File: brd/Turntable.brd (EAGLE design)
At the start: 100 x 80 mm, 115 parts, among them CON1 Pannel, CON2 CAN, CON3 Turntable, CON4 STEPPER_CON, CON5 STEPPER_CON, CON8 SPK, IC1 7805, IC2 LM393N, J1 MiniStp2, J10 MiniStp1, Q1 BS170, SW1 EC12E_SW, U2 LED NANO, X1 AK500/2+M, X2 AK500/2+M, X3 MAB 5SH Conrad: 738247 - VQ, X4 AK500/2+M, X5 Reichelt MEBP 8-8S

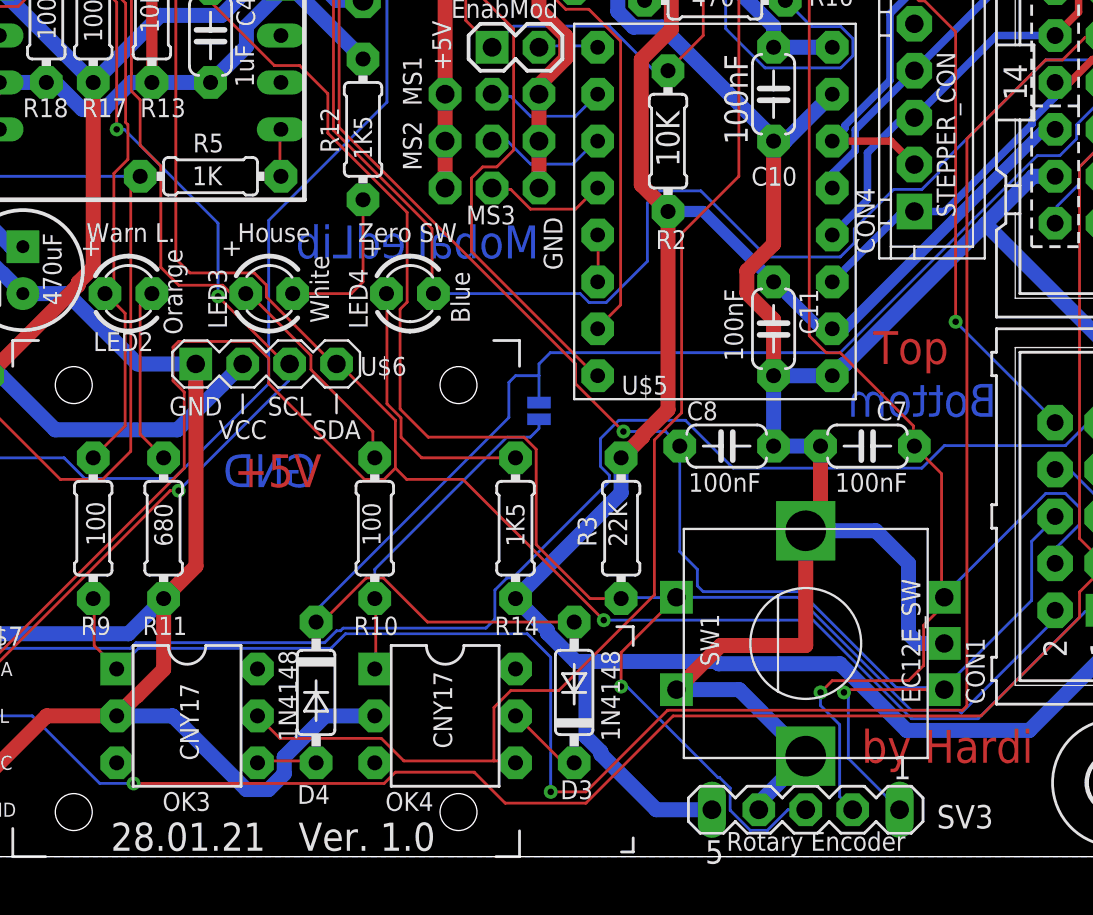
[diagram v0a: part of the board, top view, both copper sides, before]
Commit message: Corrected Potary Encoder Pins
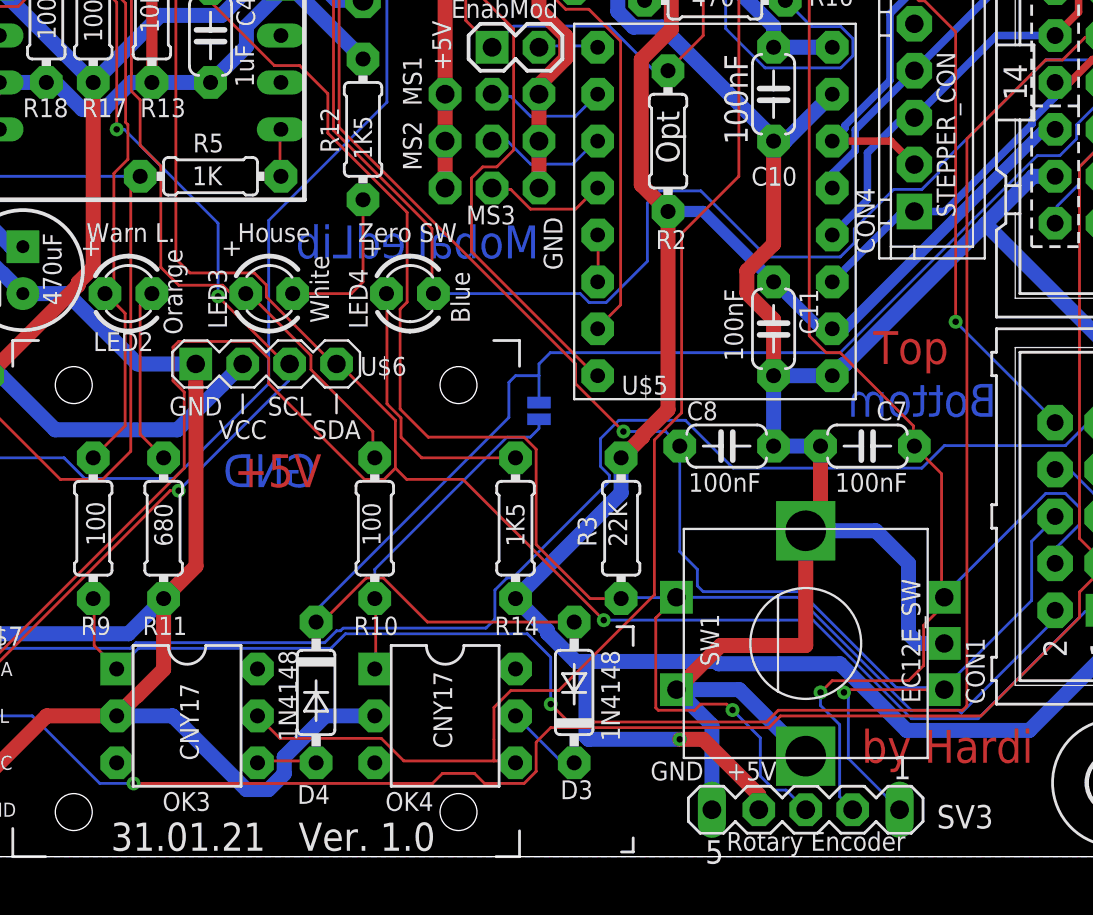
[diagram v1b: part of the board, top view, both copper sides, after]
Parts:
- R2: value 10K -> Opt
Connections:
- net +5V: now also SV3.4; no longer SV3.5
- net GND: now also SV3.5; no longer SV3.4
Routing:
- net DIR_FLASH: track 101.3 -> 95.4 mm
- net GND: track 520.2 -> 523.5 mm
- net +5V: track 396.8 -> 399.8 mm, vias 0 -> 1
- net BUTTON: track 110.2 -> 108.1 mm
